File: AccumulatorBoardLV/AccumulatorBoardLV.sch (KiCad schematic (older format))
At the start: 51 parts, among them J1 Contactor 1, J10 To HV Board, J11 IMD Reset, J12 TS Interlock, J13 Temp Reset, J14 To ECU, J15 Charger LV, J16 Charger Interlock, J17 Lid Interlock, J18 From HV Board, J19 Chip 1, J2 BMS Connector 1, J20 Chip 2, J21 Chip 3, J22 Chip 4, J3 BMS Connector 2, J4 BMS TX, J5 BMS RX, J6 Current Sensor, J7 Contactor 2, J8 IMD LV, J9 BMS Reset, U1 DE1A1B-L2-12V, U10 MCP3008, U11 ISO1050, U12 stm_nucleo_FK303K8, U13 MCP3008, U14 MCP3008, U2 LM555N, U3 SN754410, U4 DE1A1B-L2-12V, U5 L78S05CV-DG, U6 DE1A1B-L2-12V, U7 DK1A1B-12V, U8 ADUM4154ARIZ, U9 MCP3008

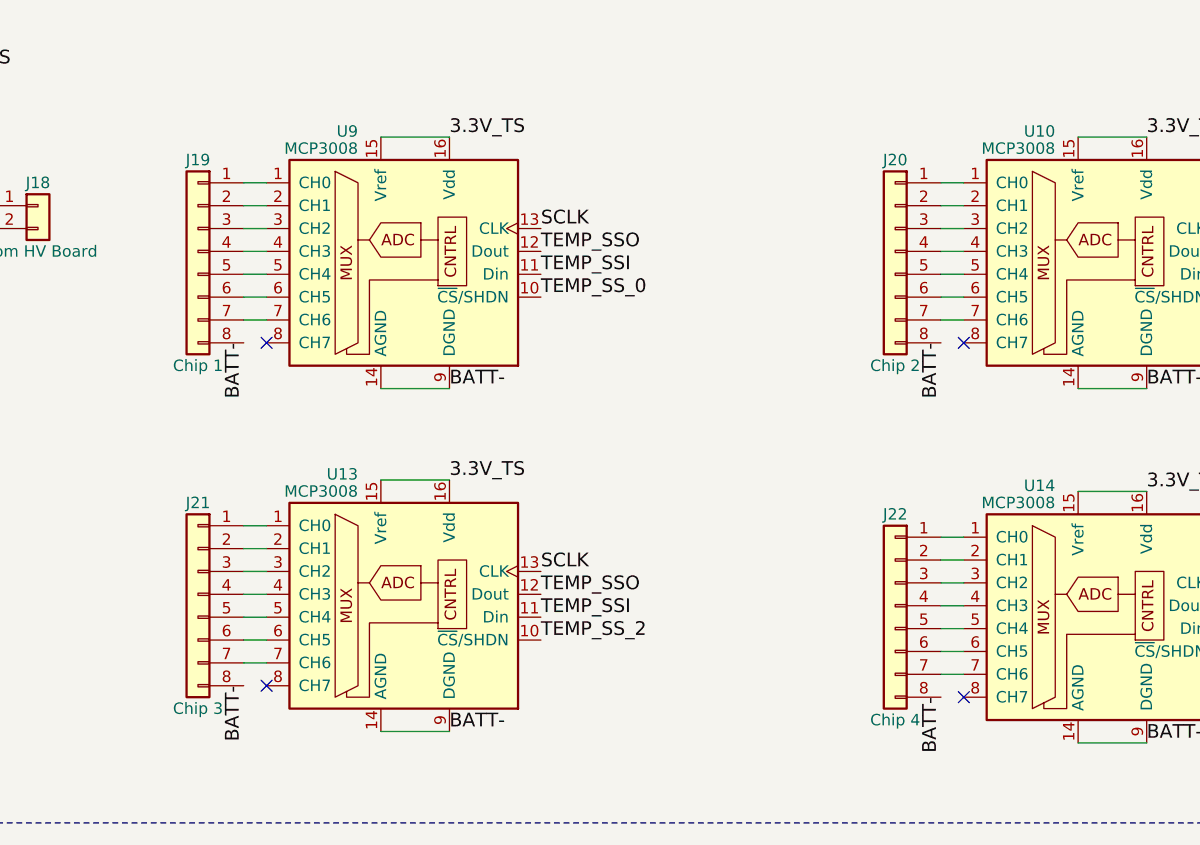
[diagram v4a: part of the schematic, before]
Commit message: Add connections to connectors on PE and Acc LV boards
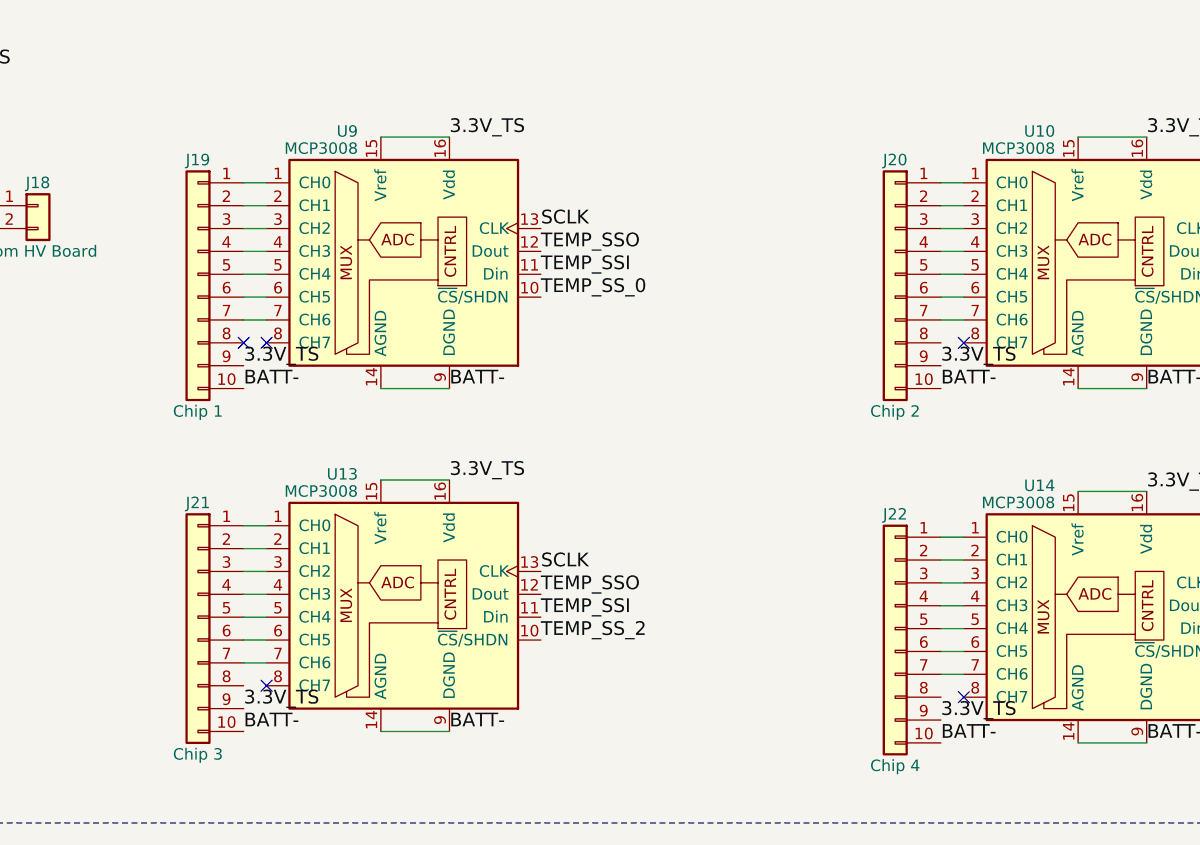
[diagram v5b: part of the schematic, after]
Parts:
- removed J19: Chip 1, Connectors_Molex:Molex_NanoFit_2x04x2.50mm_Straight, symbol Conn_01x08
- removed J20: Chip 2, Connectors_Molex:Molex_NanoFit_2x04x2.50mm_Straight, symbol Conn_01x08
- removed J21: Chip 3, Connectors_Molex:Molex_NanoFit_2x04x2.50mm_Straight, symbol Conn_01x08
- removed J22: Chip 4, Connectors_Molex:Molex_NanoFit_2x04x2.50mm_Straight, symbol Conn_01x08
- added J19: Chip 1, Connectors_Molex:Molex_NanoFit_2x05x2.50mm_Straight, symbol Conn_01x10
- added J20: Chip 2, Connectors_Molex:Molex_NanoFit_2x05x2.50mm_Straight, symbol Conn_01x10
- added J21: Chip 3, Connectors_Molex:Molex_NanoFit_2x05x2.50mm_Straight, symbol Conn_01x10
- added J22: Chip 4, Connectors_Molex:Molex_NanoFit_2x05x2.50mm_Straight, symbol Conn_01x10
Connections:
- net 3.3V_TS: now also J19.9 (Pin_9), J20.9 (Pin_9), J21.9 (Pin_9), J22.9 (Pin_9)
- net BATT-: now also J19.10 (Pin_10), J20.10 (Pin_10), J21.10 (Pin_10), J22.10 (Pin_10)
- net at U13.1 (CH0): now also J21.1 (Pin_1)
- net at U13.2 (CH1): now also J21.2 (Pin_2)
- net at U13.3 (CH2): now also J21.3 (Pin_3)
- net at U13.4 (CH3): now also J21.4 (Pin_4)
- net at U13.5 (CH4): now also J21.5 (Pin_5)
- net at U13.6 (CH5): now also J21.6 (Pin_6)
- net at U13.7 (CH6): now also J21.7 (Pin_7)
- net at U10.1 (CH0): now also J20.1 (Pin_1)
- net at U10.2 (CH1): now also J20.2 (Pin_2)
- net at U10.3 (CH2): now also J20.3 (Pin_3)
- net at U10.4 (CH3): now also J20.4 (Pin_4)
- net at U10.5 (CH4): now also J20.5 (Pin_5)
- net at U10.6 (CH5): now also J20.6 (Pin_6)
- net at U10.7 (CH6): now also J20.7 (Pin_7)
- net at U14.1 (CH0): now also J22.1 (Pin_1)
- net at U14.2 (CH1): now also J22.2 (Pin_2)
- net at U14.3 (CH2): now also J22.3 (Pin_3)
- net at U14.4 (CH3): now also J22.4 (Pin_4)
- net at U14.5 (CH4): now also J22.5 (Pin_5)
- net at U14.6 (CH5): now also J22.6 (Pin_6)
- net at U14.7 (CH6): now also J22.7 (Pin_7)
- net at U9.1 (CH0): now also J19.1 (Pin_1)
- net at U9.2 (CH1): now also J19.2 (Pin_2)
- net at U9.3 (CH2): now also J19.3 (Pin_3)
- net at U9.4 (CH3): now also J19.4 (Pin_4)
- net at U9.5 (CH4): now also J19.5 (Pin_5)
- net at U9.6 (CH5): now also J19.6 (Pin_6)
- net at U9.7 (CH6): now also J19.7 (Pin_7)
- no-connect marks 15 -> 16
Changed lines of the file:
@@
 Text Label 12950 8800 0    60   ~ 0
 TEMP_SS_3
-$Comp
-L Conn_01x08 J19
-U 1 1 59C1AEA8
-P 8400 7050
-F 0 "J19" H 8400 7450 50  0000 C CNN
-F 1 "Chip 1" H 8400 6550 50  0000 C CNN
-F 2 "Connectors_Molex:Molex_NanoFit_2x04x2.50mm_Straight" H 8400 7050 50  0001 C CNN
-F 3 "" H 8400 7050 50  0001 C CNN
-	1    8400 7050
-	-1   0    0    -1
-$EndComp
-$Comp
-L Conn_01x08 J21
-U 1 1 59C1AF7F
-P 8400 8550
-F 0 "J21" H 8400 8950 50  0000 C CNN
-F 1 "Chip 3" H 8400 8050 50  0000 C CNN
-F 2 "Connectors_Molex:Molex_NanoFit_2x04x2.50mm_Straight" H 8400 8550 50  0001 C CNN
-F 3 "" H 8400 8550 50  0001 C CNN
-	1    8400 8550
-	-1   0    0    -1
-$EndComp
-$Comp
-L Conn_01x08 J20
-U 1 1 59C1B02E
-P 11450 7050
-F 0 "J20" H 11450 7450 50  0000 C CNN
-F 1 "Chip 2" H 11450 6550 50  0000 C CNN
-F 2 "Connectors_Molex:Molex_NanoFit_2x04x2.50mm_Straight" H 11450 7050 50  0001 C CNN
-F 3 "" H 11450 7050 50  0001 C CNN
-	1    11450 7050
-	-1   0    0    -1
-$EndComp
-$Comp
-L Conn_01x08 J22
-U 1 1 59C1B0E4
-P 11450 8600
-F 0 "J22" H 11450 9000 50  0000 C CNN
-F 1 "Chip 4" H 11450 8100 50  0000 C CNN
-F 2 "Connectors_Molex:Molex_NanoFit_2x04x2.50mm_Straight" H 11450 8600 50  0001 C CNN
-F 3 "" H 11450 8600 50  0001 C CNN
-	1    11450 8600
-	-1   0    0    -1
-$EndComp
 Text Notes 5900 5850 0    60   ~ 0
 Temp System
@@
 Wire Wire Line
 	8700 7350 8600 7350
-Text Label 8600 7450 3    60   ~ 0
+Text Label 8600 7650 0    60   ~ 0
 BATT-
 Wire Wire Line
@@
 Wire Wire Line
 	8600 8850 8700 8850
-Text Label 8600 8950 3    60   ~ 0
+Text Label 8600 9150 0    60   ~ 0
 BATT-
 Wire Wire Line
@@
 Wire Wire Line
 	11650 8900 11750 8900
-Text Label 11650 9000 3    60   ~ 0
-BATT-
-Text Label 11650 7450 3    60   ~ 0
+Text Label 11650 9200 0    60   ~ 0
+BATT-
+Text Label 11650 7650 0    60   ~ 0
 BATT-
 NoConn ~ 11750 7450
@@
 NoConn ~ 8700 8950
 NoConn ~ 8700 7450
+$Comp
+L Conn_01x10 J19
+U 1 1 5AA89576
+P 8400 7150
+F 0 "J19" H 8400 7650 50  0000 C CNN
+F 1 "Chip 1" H 8400 6550 50  0000 C CNN
+F 2 "Connectors_Molex:Molex_NanoFit_2x05x2.50mm_Straight" H 8400 7150 50  0001 C CNN
+F 3 "" H 8400 7150 50  0001 C CNN
+	1    8400 7150
+	-1   0    0    -1
+$EndComp
+Text Label 8600 7550 0    60   ~ 0
+3.3V_TS
+NoConn ~ 8600 7450
+$Comp
+L Conn_01x10 J20
+U 1 1 5AA89A40
+P 11450 7150
+F 0 "J20" H 11450 7650 50  0000 C CNN
+F 1 "Chip 2" H 11450 6550 50  0000 C CNN
+F 2 "Connectors_Molex:Molex_NanoFit_2x05x2.50mm_Straight" H 11450 7150 50  0001 C CNN
+F 3 "" H 11450 7150 50  0001 C CNN
+	1    11450 7150
+	-1   0    0    -1
+$EndComp
+Text Label 11650 7550 0    60   ~ 0
+3.3V_TS
+$Comp
+L Conn_01x10 J21
+U 1 1 5AA8AACD
+P 8400 8650
+F 0 "J21" H 8400 9150 50  0000 C CNN
+F 1 "Chip 3" H 8400 8050 50  0000 C CNN
+F 2 "Connectors_Molex:Molex_NanoFit_2x05x2.50mm_Straight" H 8400 8650 50  0001 C CNN
+F 3 "" H 8400 8650 50  0001 C CNN
+	1    8400 8650
+	-1   0    0    -1
+$EndComp
+Text Label 8600 9050 0    60   ~ 0
+3.3V_TS
+$Comp
+L Conn_01x10 J22
+U 1 1 5AA8B655
+P 11450 8700
+F 0 "J22" H 11450 9200 50  0000 C CNN
+F 1 "Chip 4" H 11450 8100 50  0000 C CNN
+F 2 "Connectors_Molex:Molex_NanoFit_2x05x2.50mm_Straight" H 11450 8700 50  0001 C CNN
+F 3 "" H 11450 8700 50  0001 C CNN
+	1    11450 8700
+	-1   0    0    -1
+$EndComp
+Text Label 11650 9100 0    60   ~ 0
+3.3V_TS
 $EndSCHEMATC

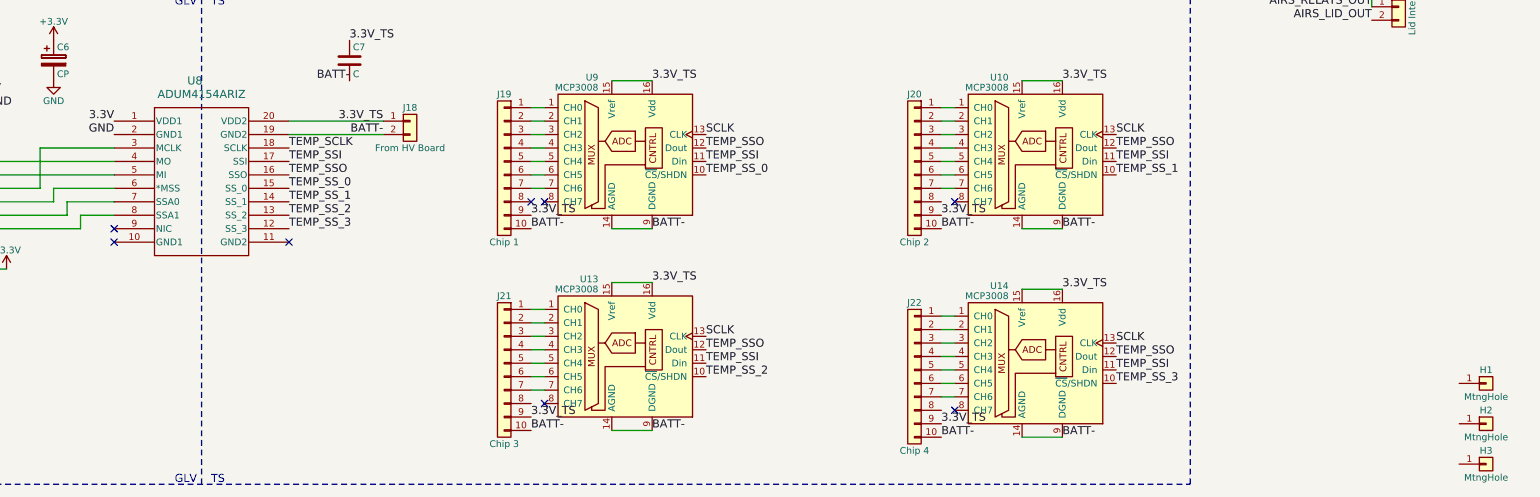
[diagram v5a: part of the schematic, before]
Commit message: redo AccumulatorBoardLV for new accumulator packaging scheme
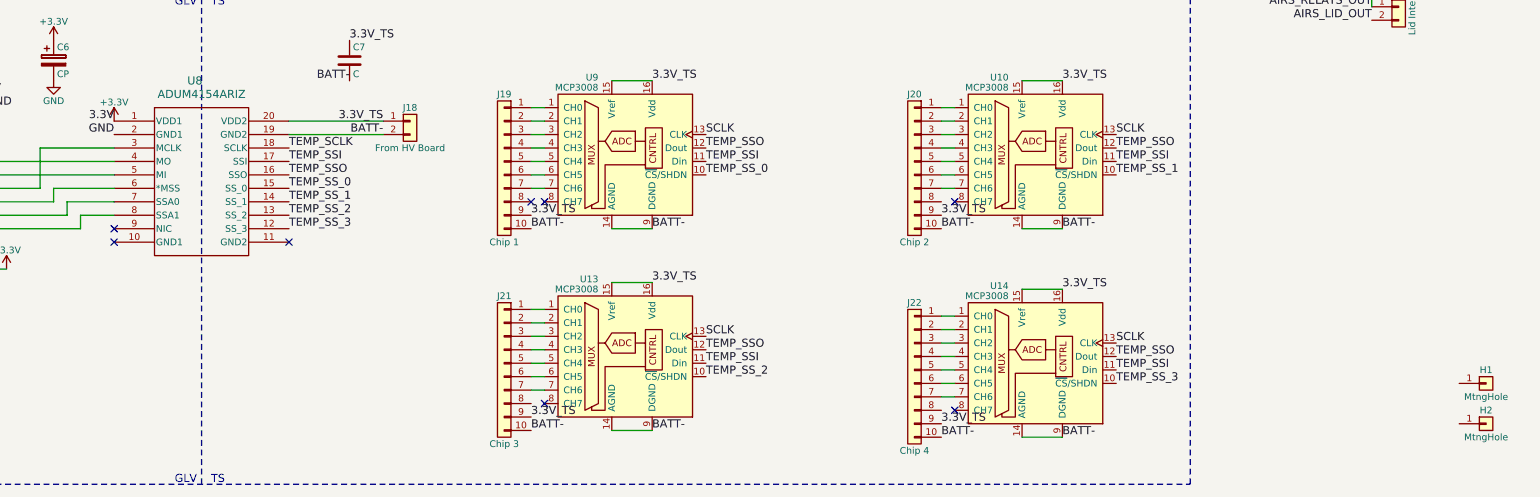
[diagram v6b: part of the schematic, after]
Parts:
- removed H3: MtngHole, Mounting_Holes:MountingHole_4.5mm, symbol Conn_01x01
- J14: footprint FSFootprints:Ampseal - 14 pin -> FSFootprints:Ampseal-776261
- J15: footprint FSFootprints:Ampseal - 8 pin -> FSFootprints:Ampseal-776276-1
- U10, U13, U14, U9: footprint Housings_DIP:DIP-16_W7.62mm -> Housings_SOIC:SOIC-16_3.9x9.9mm_Pitch1.27mm
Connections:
- net 3.3V is gone; now on net +3V3: U8.1 (VDD1)
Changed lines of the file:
@@
 F 0 "J15" H 5850 5350 50  0000 C CNN
 F 1 "Charger LV" V 5950 4900 50  0000 C CNN
-F 2 "FSFootprints:Ampseal - 8 pin" H 5850 4900 50  0001 C CNN
+F 2 "FSFootprints:Ampseal-776276-1" H 5850 4900 50  0001 C CNN
 F 3 "" H 5850 4900 50  0001 C CNN
 	1    5850 4900
@@
 F 0 "J14" H 4400 5650 50  0000 C CNN
 F 1 "To ECU" V 4500 4900 50  0000 C CNN
-F 2 "FSFootprints:Ampseal - 14 pin" H 4400 4900 50  0001 C CNN
+F 2 "FSFootprints:Ampseal-776261" H 4400 4900 50  0001 C CNN
 F 3 "" H 4400 4900 50  0000 C CNN
 	1    4400 4900
@@
 F 0 "U13" H 9100 9075 50  0000 R CNN
 F 1 "MCP3008" H 9100 9000 50  0000 R CNN
-F 2 "Housings_DIP:DIP-16_W7.62mm" H 9400 8650 50  0001 C CNN
+F 2 "Housings_SOIC:SOIC-16_3.9x9.9mm_Pitch1.27mm" H 9400 8650 50  0001 C CNN
 F 3 "" H 9400 8650 50  0001 C CNN
 	1    9300 8550
@@
 F 0 "U10" H 12150 7575 50  0000 R CNN
 F 1 "MCP3008" H 12150 7500 50  0000 R CNN
-F 2 "Housings_DIP:DIP-16_W7.62mm" H 12450 7150 50  0001 C CNN
+F 2 "Housings_SOIC:SOIC-16_3.9x9.9mm_Pitch1.27mm" H 12450 7150 50  0001 C CNN
 F 3 "" H 12450 7150 50  0001 C CNN
 	1    12350 7050
@@
 F 0 "U14" H 12150 9125 50  0000 R CNN
 F 1 "MCP3008" H 12150 9050 50  0000 R CNN
-F 2 "Housings_DIP:DIP-16_W7.62mm" H 12450 8700 50  0001 C CNN
+F 2 "Housings_SOIC:SOIC-16_3.9x9.9mm_Pitch1.27mm" H 12450 8700 50  0001 C CNN
 F 3 "" H 12450 8700 50  0001 C CNN
 	1    12350 8600
@@
 F 0 "U9" H 9100 7575 50  0000 R CNN
 F 1 "MCP3008" H 9100 7500 50  0000 R CNN
-F 2 "Housings_DIP:DIP-16_W7.62mm" H 9400 7150 50  0001 C CNN
+F 2 "Housings_SOIC:SOIC-16_3.9x9.9mm_Pitch1.27mm" H 9400 7150 50  0001 C CNN
 F 3 "" H 9400 7150 50  0001 C CNN
 	1    9300 7050
@@
 	1    0    0    -1
 $EndComp
-$Comp
-L Conn_01x01 H3
-U 1 1 5A97E02C
-P 15700 9400
-F 0 "H3" H 15700 9500 50  0000 C CNN
-F 1 "MtngHole" H 15700 9300 50  0000 C CNN
-F 2 "Mounting_Holes:MountingHole_4.5mm" H 15700 9400 50  0001 C CNN
-F 3 "" H 15700 9400 50  0001 C CNN
-	1    15700 9400
-	1    0    0    -1
-$EndComp
 Text Label 14850 6000 2    60   ~ 0
 AIRS_RELAYS_OUT
@@
 Text Label 11650 9100 0    60   ~ 0
 3.3V_TS
+$Comp
+L +3.3V #PWR?
+U 1 1 5AAB30E7
+P 5500 6850
+F 0 "#PWR?" H 5500 6700 50  0001 C CNN
+F 1 "+3.3V" H 5500 6990 50  0000 C CNN
+F 2 "" H 5500 6850 50  0001 C CNN
+F 3 "" H 5500 6850 50  0001 C CNN
+	1    5500 6850
+	1    0    0    -1
+$EndComp
 $EndSCHEMATC

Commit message: edit PCBs based on actual parts that have arrived
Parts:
- U11: footprint SMD_Packages:DIP-8_SMD -> Housings_DIP:DIP-8_W8.89mm_SMDSocket_LongPads
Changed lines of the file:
@@
 F 0 "U11" H 1700 7300 60  0000 C CNN
 F 1 "ISO1050" H 1400 7300 60  0000 C CNN
-F 2 "SMD_Packages:DIP-8_SMD" H 1450 6600 60  0001 C CNN
+F 2 "Housings_DIP:DIP-8_W8.89mm_SMDSocket_LongPads" H 1450 6600 60  0001 C CNN
 F 3 "" H 1400 7300 60  0000 C CNN
 	1    1450 7300
@@
 3.3V_TS
 $Comp
-L +3.3V #PWR?
+L +3.3V #PWR035
 U 1 1 5AAB30E7
 P 5500 6850
-F 0 "#PWR?" H 5500 6700 50  0001 C CNN
+F 0 "#PWR035" H 5500 6700 50  0001 C CNN
 F 1 "+3.3V" H 5500 6990 50  0000 C CNN
 F 2 "" H 5500 6850 50  0001 C CNN

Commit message: prepare to re-send PE LV board
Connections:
- net TEMP_SCLK is gone; now on net SCLK: U8.18 (SCLK)
- net +12V: now also U12.30 (VIN)
- net +5V: no longer U12.30 (VIN)
- net BATT-: now also U8.11 (GND2)
- net GND: now also U8.10 (GND1)
- net CAN_RX: now reaches U11.2 (RXD), U12.14 (D11)
- net CAN_TX: now reaches U11.3 (TXD), U12.5 (D2)
- no-connect marks 16 -> 14
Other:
- moved on the sheet: H1, H2
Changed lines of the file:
@@
 GND
 Text Label 4550 6650 0    60   ~ 0
-5V
+12V
 Text Label 3250 6950 2    60   ~ 0
 GND
@@
 $EndComp
 NoConn ~ 5500 7650
-NoConn ~ 5500 7750
 $Comp
 L Conn_01x02 J18
@@
 BATT-
 Text Label 6800 7050 0    60   ~ 0
-TEMP_SCLK
+SCLK
 Text Label 6800 7150 0    60   ~ 0
 TEMP_SSI
@@
 Text Label 6800 7650 0    60   ~ 0
 TEMP_SS_3
-NoConn ~ 6800 7750
 $Comp
 L MCP3008 U13
@@
 L Conn_01x01 H1
 U 1 1 5A97D013
-P 15700 8800
-F 0 "H1" H 15700 8900 50  0000 C CNN
-F 1 "MtngHole" H 15700 8700 50  0000 C CNN
-F 2 "Mounting_Holes:MountingHole_4.5mm" H 15700 8800 50  0001 C CNN
-F 3 "" H 15700 8800 50  0001 C CNN
-	1    15700 8800
+P 17300 8800
+F 0 "H1" H 17300 8900 50  0000 C CNN
+F 1 "MtngHole" H 17300 8700 50  0000 C CNN
+F 2 "Mounting_Holes:MountingHole_4.5mm" H 17300 8800 50  0001 C CNN
+F 3 "" H 17300 8800 50  0001 C CNN
+	1    17300 8800
 	1    0    0    -1
 $EndComp
@@
 L Conn_01x01 H2
 U 1 1 5A97DEDA
-P 15700 9100
-F 0 "H2" H 15700 9200 50  0000 C CNN
-F 1 "MtngHole" H 15700 9000 50  0000 C CNN
-F 2 "Mounting_Holes:MountingHole_4.5mm" H 15700 9100 50  0001 C CNN
-F 3 "" H 15700 9100 50  0001 C CNN
-	1    15700 9100
+P 17300 9100
+F 0 "H2" H 17300 9200 50  0000 C CNN
+F 1 "MtngHole" H 17300 9000 50  0000 C CNN
+F 2 "Mounting_Holes:MountingHole_4.5mm" H 17300 9100 50  0001 C CNN
+F 3 "" H 17300 9100 50  0001 C CNN
+	1    17300 9100
 	1    0    0    -1
 $EndComp
@@
 	1    0    0    -1
 $EndComp
+Text Label 6800 7750 0    60   ~ 0
+BATT-
+Text Label 5500 7750 2    60   ~ 0
+GND
+Text Label 3250 7050 2    60   ~ 0
+CAN_TX
+Text Label 3250 7950 2    60   ~ 0
+CAN_RX
 $EndSCHEMATC
